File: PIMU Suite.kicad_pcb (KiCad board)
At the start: 2 copper layers, 77 x 50.5 mm, 16 parts, among them U2 MICROSD_SPI_OR_SDIO_CARD

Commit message: Final updates
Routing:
- net /SD_SCK: track 28.5 -> 28.7 mm, vias 2 -> 1
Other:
- board text added: "Made with <3"
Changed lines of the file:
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@@
+		)
+	)
+	(gr_text "Made with <3"
+		(at 181.5 75 0)
+		(layer "B.SilkS")
+		(effects
+			(font
+				(face "Monocraft Nerd Font")
+				(size 1 1)
+				(thickness 0.2)
+				(bold yes)
+			)
+			(justify left bottom mirror)
+		)
+		(render_cache "Made with <3" 0
+			(polygon
+				(pts
+					(xy 181.531263 74.861263) (xy 181.531263 73.708436) (xy 181.313459 73.708436) (xy 181.313459 73.86579)
+					(xy 181.159281 73.86579) (xy 181.159281 74.021067) (xy 181.065919 74.021067) (xy 181.065919 73.86579)
+					(xy 180.908871 73.86579) (xy 180.908871 73.708436) (xy 180.691067 73.708436) (xy 180.691067 74.861263)
+					(xy 180.908871 74.861263) (xy 180.908871 74.083593) (xy 181.003698 74.083593) (xy 181.003698 74.238871)
+					(xy 181.221502 74.238871) (xy 181.221502 74.083593) (xy 181.313459 74.083593) (xy 181.313459 74.861263)
+				)
+			)
+			(polygon
+				(pts
+					(xy 180.441939 74.238871) (xy 179.975863 74.238871) (xy 179.975863 74.333698) (xy 180.441939 74.333698)
+					(xy 180.441939 74.487144) (xy 180.598255 74.487144) (xy 180.598255 74.704947) (xy 180.441939 74.704947)
+					(xy 180.441939 74.861263) (xy 179.75806 74.861263) (xy 179.75806 74.643459) (xy 179.975863 74.643459)
+					(xy 180.380451 74.643459) (xy 180.380451 74.551502) (xy 179.975863 74.551502) (xy 179.975863 74.643459)
+					(xy 179.75806 74.643459) (xy 179.75806 74.176589) (xy 179.914375 74.176589) (xy 179.914375 74.021067)
+					(xy 180.441939 74.021067)
+				)
+			)
+			(polygon
+				(pts
+					(xy 179.042855 74.177383) (xy 179.133775 74.177383) (xy 179.133775 74.021067) (xy 179.508932 74.021067)
+					(xy 179.508932 74.177383) (xy 179.665247 74.177383) (xy 179.665247 74.704947) (xy 179.508932 74.704947)
+					(xy 179.508932 74.861263) (xy 178.825052 74.861263) (xy 178.825052 74.395186) (xy 179.042855 74.395186)
+					(xy 179.042855 74.643459) (xy 179.447444 74.643459) (xy 179.447444 74.238871) (xy 179.196484 74.238871)
+					(xy 179.196484 74.395186) (xy 179.042855 74.395186) (xy 178.825052 74.395186) (xy 178.825052 73.708436)
+					(xy 179.042855 73.708436)
+				)
+			)
+			(polygon
+				(pts
+					(xy 178.575924 74.177383) (xy 178.73224 74.177383) (xy 178.73224 74.704947) (xy 178.575924 74.704947)
+					(xy 178.575924 74.861263) (xy 177.892044 74.861263) (xy 177.892044 74.643459) (xy 178.514436 74.643459)
+					(xy 178.514436 74.551502) (xy 177.892044 74.551502) (xy 177.892044 74.333698) (xy 178.109848 74.333698)
+					(xy 178.514436 74.333698) (xy 178.514436 74.238871) (xy 178.109848 74.238871) (xy 178.109848 74.333698)
+					(xy 177.892044 74.333698) (xy 177.892044 74.177383) (xy 178.04836 74.177383) (xy 178.04836 74.021067)
+					(xy 178.575924 74.021067)
+				)
+			)
+			(polygon
+				(pts
+					(xy 176.710642 74.861263) (xy 176.710642 74.704947) (xy 176.866224 74.704947) (xy 176.866224 74.021067)
+					(xy 176.648421 74.021067) (xy 176.648421 74.643459) (xy 176.556463 74.643459) (xy 176.556463 74.332233)
+					(xy 176.33866 74.332233) (xy 176.33866 74.643459) (xy 176.243832 74.643459) (xy 176.243832 74.021067)
+					(xy 176.026029 74.021067) (xy 176.026029 74.861263)
+				)
+			)
+			(polygon
+				(pts
+					(xy 175.698743 73.92624) (xy 175.698743 73.708436) (xy 175.48094 73.708436) (xy 175.48094 73.92624)
+				)
+			)
+			(polygon
+				(pts
+					(xy 175.542428 74.861263) (xy 175.542428 74.70568) (xy 175.698743 74.70568) (xy 175.698743 74.238871)
+					(xy 175.855059 74.238871) (xy 175.855059 74.021067) (xy 175.48094 74.021067) (xy 175.48094 74.643459)
+					(xy 175.167271 74.643459) (xy 175.167271 74.861263)
+				)
+			)
+			(polygon
+				(pts
+					(xy 174.613328 74.861263) (xy 174.613328 74.704947) (xy 174.765736 74.704947) (xy 174.765736 74.238871)
+					(xy 174.922051 74.238871) (xy 174.922051 74.021067) (xy 174.765736 74.021067) (xy 174.765736 73.708436)
+					(xy 174.547932 73.708436) (xy 174.547932 74.021067) (xy 174.394487 74.021067) (xy 174.394487 74.238871)
+					(xy 174.547932 74.238871) (xy 174.547932 74.643459) (xy 174.238171 74.643459) (xy 174.238171 74.861263)
+				)
+			)
+			(polygon
+				(pts
+					(xy 174.067201 74.861263) (xy 174.067201 73.708436) (xy 173.849398 73.708436) (xy 173.849398 74.177383)
+					(xy 173.758478 74.177383) (xy 173.758478 74.021067) (xy 173.383321 74.021067) (xy 173.383321 74.177383)
+					(xy 173.227006 74.177383) (xy 173.227006 74.861263) (xy 173.444809 74.861263) (xy 173.444809 74.238871)
+					(xy 173.695769 74.238871) (xy 173.695769 74.395186) (xy 173.849398 74.395186) (xy 173.849398 74.861263)
+				)
+			)
+			(polygon
+				(pts
+					(xy 171.735109 74.861263) (xy 171.735109 74.704947) (xy 171.891425 74.704947) (xy 171.891425 74.551502)
+					(xy 172.04487 74.551502) (xy 172.04487 74.395186) (xy 172.201186 74.395186) (xy 172.201186 74.177383)
+					(xy 172.04487 74.177383) (xy 172.04487 74.021067) (xy 171.891425 74.021067) (xy 171.891425 73.86579)
+					(xy 171.735109 73.86579) (xy 171.735109 73.708436) (xy 171.517306 73.708436) (xy 171.517306 73.92624)
+					(xy 171.673621 73.92624) (xy 171.673621 74.083593) (xy 171.827067 74.083593) (xy 171.827067 74.238871)
+					(xy 171.983382 74.238871) (xy 171.983382 74.333698) (xy 171.827067 74.333698) (xy 171.827067 74.487144)
+					(xy 171.673621 74.487144) (xy 171.673621 74.643459) (xy 171.517306 74.643459) (xy 171.517306 74.861263)
+				)
+			)
+			(polygon
+				(pts
+					(xy 171.111863 74.861263) (xy 171.111863 74.704947) (xy 171.268178 74.704947) (xy 171.268178 74.487144)
+					(xy 171.050375 74.487144) (xy 171.050375 74.643459) (xy 170.645786 74.643459) (xy 170.645786 74.395186)
+					(xy 170.959455 74.395186) (xy 170.959455 74.177383) (xy 170.645786 74.177383) (xy 170.645786 73.92624)
+					(xy 171.050375 73.92624) (xy 171.050375 74.082555) (xy 171.268178 74.082555) (xy 171.268178 73.864752)
+					(xy 171.111863 73.864752) (xy 171.111863 73.708436) (xy 170.584298 73.708436) (xy 170.584298 73.864752)
+					(xy 170.427983 73.864752) (xy 170.427983 74.239909) (xy 170.584298 74.239909) (xy 170.584298 74.32979)
+					(xy 170.427983 74.32979) (xy 170.427983 74.704947) (xy 170.584298 74.704947) (xy 170.584298 74.861263)
+				)
+			)
+		)
+	)
+	(gr_text_box "Next version:\n- Add silkscreen names to each pin\n- Cleanup routes\n- Change meme"
+		(start 130.125 61.375)
+		(end 164.375 69.625)
+		(margins 1.0025 1.0025 1.0025 1.0025)
+		(layer "F.Fab")
+		(effects
+			(font
+				(size 1 1)
+				(thickness 0.2)
+				(bold yes)
+			)
+			(justify left top)
+		)
+		(border yes)
+		(stroke
+			(width 0.2)
+			(type solid)
 		)
 	)
@@
 	)
 	(segment
-		(start 131.5 95.5)
-		(end 131.75 95.25)
-		(width 0.2)
-		(layer "F.Cu")
-		(net 19)
-	)
-	(segment
 		(start 131.75 89.93)
 		(end 143.22 78.46)
@@
 	)
 	(segment
-		(start 127.08 99.92)
-		(end 127.875 99.125)
-		(width 0.2)
-		(layer "F.Cu")
-		(net 19)
-	)
-	(segment
 		(start 131.75 95.25)
 		(end 131.75 89.93)
@@
 	)
 	(via
-		(at 127.875 99.125)
+		(at 131.75 95.25)
 		(size 0.7)
 		(drill 0.3)
@@
 		(net 19)
 	)
-	(via
-		(at 131.5 95.5)
-		(size 0.6)
-		(drill 0.3)
-		(layers "F.Cu" "B.Cu")
-		(net 19)
-	)
-	(segment
-		(start 127.875 99.125)
-		(end 131.5 95.5)
+	(segment
+		(start 131.75 95.25)
+		(end 131.75 95.44)
 		(width 0.2)
 		(layer "B.Cu")
@@
 		(width 0.2)
 		(layer "B.Cu")
+		(net 19)
+	)
+	(segment
+		(start 131.75 95.44)
+		(end 127.08 100.11)
+		(width 0.2)
+		(layer "B.Cu")

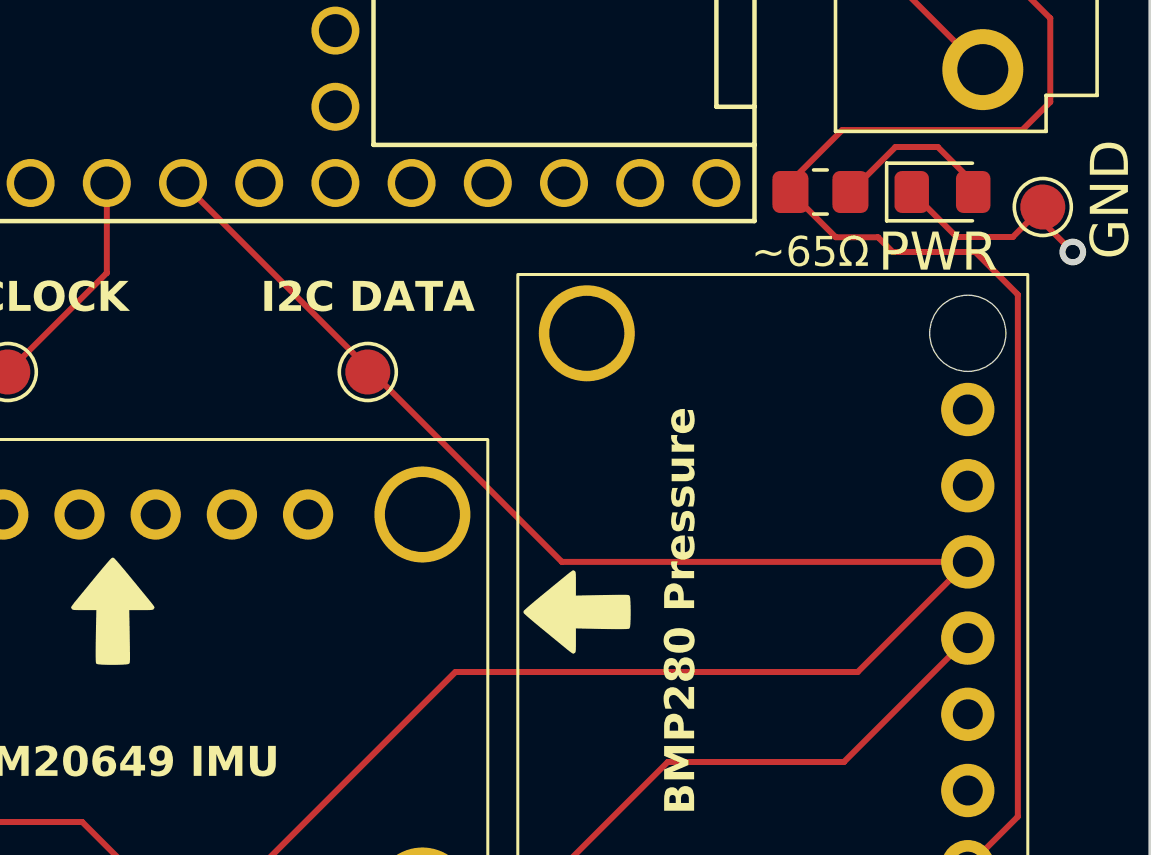
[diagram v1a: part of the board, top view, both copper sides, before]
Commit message: Fix wrong wiring
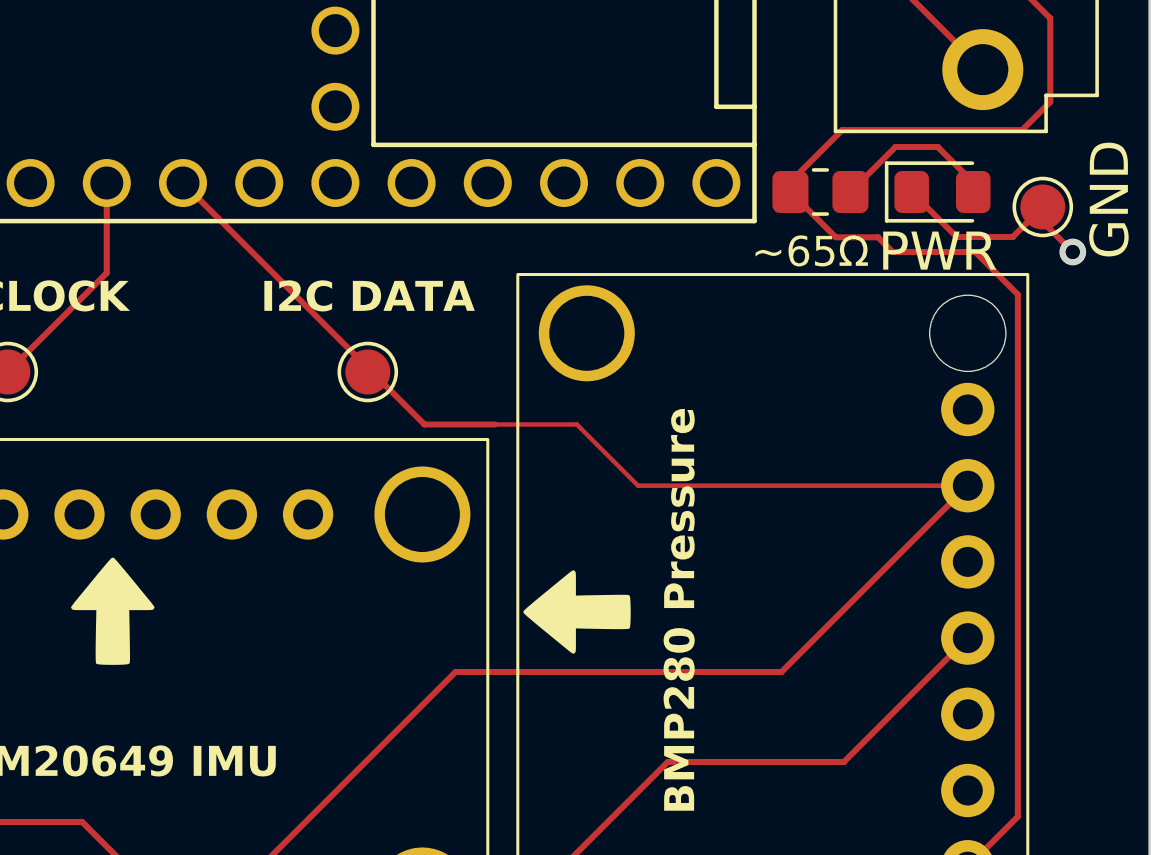
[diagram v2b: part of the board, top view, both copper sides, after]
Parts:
- JST1: value JST -> S4B-XH-A-1
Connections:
- BMP1 pad 5: /SDA_LINE -> unconnected-(BMP1-SDO-Pad5)
- BMP1 pad 6: unconnected-(BMP1-SDI-Pad6) -> /SDA_LINE
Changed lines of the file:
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@@
 	(net 68 "unconnected-(TEENSY1-GND-Pad58)")
 	(net 69 "unconnected-(U2-DAT2-Pad8)")
-	(net 70 "unconnected-(BMP1-SDI-Pad6)")
+	(net 70 "unconnected-(BMP1-SDO-Pad5)")
 	(net 71 "unconnected-(U2-DAT1-Pad7)")
 	(net 72 "unconnected-(TEENSY1-T--Pad62)")
@@
 			)
 		)
-		(property "Value" "JST"
+		(property "Value" "S4B-XH-A-1"
 			(at 5.94 6 90)
 			(layer "F.Fab")
@@
 			(layers "*.Cu" "*.Mask")
 			(remove_unused_layers no)
-			(net 11 "/SDA_LINE")
+			(net 70 "unconnected-(BMP1-SDO-Pad5)")
 			(pinfunction "SDO")
 			(pintype "output")
@@
 			(layers "*.Cu" "*.Mask")
 			(remove_unused_layers no)
-			(net 70 "unconnected-(BMP1-SDI-Pad6)")
+			(net 11 "/SDA_LINE")
 			(pinfunction "SDI")
 			(pintype "input")
@@
 	)
 	(segment
-		(start 177 106.33)
-		(end 173.33 110)
+		(start 150.84 93.7)
+		(end 158.89 101.75)
 		(width 0.2)
 		(layer "F.Cu")
@@
 	)
 	(segment
-		(start 150.84 93.7)
-		(end 163.47 106.33)
+		(start 159.92 110)
+		(end 152.47 117.45)
 		(width 0.2)
 		(layer "F.Cu")
@@
 	)
 	(segment
-		(start 159.92 110)
-		(end 152.47 117.45)
-		(width 0.2)
+		(start 161.25 101.75)
+		(end 163.97 101.75)
+		(width 0.15)
 		(layer "F.Cu")
 		(net 11)
 	)
 	(segment
-		(start 177 106.33)
-		(end 177 106)
+		(start 158.89 101.75)
+		(end 161.25 101.75)
 		(width 0.2)
 		(layer "F.Cu")
@@
 	)
 	(segment
-		(start 173.33 110)
+		(start 166.01 103.79)
+		(end 177 103.79)
+		(width 0.15)
+		(layer "F.Cu")
+		(net 11)
+	)
+	(segment
+		(start 170.79 110)
 		(end 159.92 110)
 		(width 0.2)
@@
 	)
 	(segment
-		(start 163.47 106.33)
-		(end 177 106.33)
+		(start 177 103.79)
+		(end 170.79 110)
 		(width 0.2)
 		(layer "F.Cu")
@@
 	)
 	(segment
+		(start 163.97 101.75)
+		(end 166.01 103.79)
+		(width 0.15)
+		(layer "F.Cu")
+		(net 11)
+	)
+	(segment
 		(start 127.08 100.11)
 		(end 127.08 99.92)
@@
 	)
 	(segment
+		(start 177 106.33)
+		(end 177 106)
+		(width 0.2)
+		(layer "F.Cu")
+		(net 70)
+	)
+	(segment

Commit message: JLCPCB specs
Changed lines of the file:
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@@
 		)
 		(pad_to_mask_clearance 0)
+		(solder_mask_min_width 0.12)
 		(allow_soldermask_bridges_in_footprints no)
 		(tenting front back)
 		(pcbplotparams
 			(layerselection 0x00000000_00000000_55555555_5755f5ff)
-			(plot_on_all_layers_selection 0x00000000_00000000_00000000_0200a0af)
+			(plot_on_all_layers_selection 0x00000000_00000000_00000000_00000000)
 			(disableapertmacros no)
 			(usegerberextensions no)
@@
 			(dashed_line_gap_ratio 3.000000)
 			(svgprecision 4)
-			(plotframeref yes)
+			(plotframeref no)
 			(mode 1)
 			(useauxorigin no)
@@
 			(pdf_back_fp_property_popups yes)
 			(pdf_metadata yes)
-			(pdf_single_document yes)
+			(pdf_single_document no)
 			(dxfpolygonmode yes)
 			(dxfimperialunits yes)
@@
 			(psnegative no)
 			(psa4output no)
-			(plot_black_and_white no)
+			(plot_black_and_white yes)
 			(sketchpadsonfab no)
 			(plotpadnumbers no)
@@
 			(crossoutdnponfab yes)
 			(subtractmaskfromsilk no)
-			(outputformat 4)
+			(outputformat 1)
 			(mirror no)
 			(drillshape 0)
 			(scaleselection 1)
-			(outputdirectory "Board Versions/")
+			(outputdirectory "Drills/")
 		)
 	)
@@
 				(font
 					(size 1 1)
-					(thickness 0.125)
+					(thickness 0.15)
 				)
 			)
@@
 		(effects
 			(font
-				(size 0.8 0.8)
+				(size 1 1)
 				(thickness 0.1875)
 				(bold yes)
@@
 		(effects
 			(font
-				(size 0.8 0.8)
+				(size 1 1)
 				(thickness 0.1875)
 				(bold yes)
@@
 	)
 	(segment
+		(start 131.75 95.44)
+		(end 131.75 89.93)
+		(width 0.2)
+		(layer "F.Cu")
+		(net 19)
+	)
+	(segment
 		(start 127.08 100.11)
 		(end 127.08 99.92)
@@
 	)
 	(segment
-		(start 131.75 89.93)
-		(end 143.22 78.46)
+		(start 131.47 95.72)
+		(end 131.75 95.44)
 		(width 0.2)
 		(layer "F.Cu")
@@
 	)
 	(segment
-		(start 131.75 95.25)
-		(end 131.75 89.93)
+		(start 131.75 89.93)
+		(end 143.22 78.46)
 		(width 0.2)
 		(layer "F.Cu")
@@
 	)
 	(via
-		(at 131.75 95.25)
+		(at 131.47 95.72)
 		(size 0.7)
 		(drill 0.3)
@@
 	)
 	(segment
-		(start 131.75 95.25)
-		(end 131.75 95.44)
+		(start 131.47 95.72)
+		(end 127.08 100.11)
 		(width 0.2)
 		(layer "B.Cu")
@@
 		(width 0.2)
 		(layer "B.Cu")
-		(net 19)
-	)
-	(segment
-		(start 131.75 95.44)
-		(end 127.08 100.11)
-		(width 0.2)
-		(layer "B.Cu")

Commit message: Fillits and bore holes:
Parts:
- added REF**: MountingHole_2.7mm_M2.5, MountingHole:MountingHole_2.7mm_M2.5, F.Cu at (188.5, 131.5)
- added REF**: MountingHole_2.7mm_M2.5, MountingHole:MountingHole_2.7mm_M2.5, F.Cu at (104.5, 71.5)
- added REF**: MountingHole_2.7mm_M2.5, MountingHole:MountingHole_2.7mm_M2.5, F.Cu at (188.5, 71.5)
- added REF**: MountingHole_2.7mm_M2.5, MountingHole:MountingHole_2.7mm_M2.5, F.Cu at (104.5, 131.5)
- moved G*** 4.82 mm to (111.1, 79.2)
- moved G*** 4.82 mm to (123.6, 122.2)
- moved G*** 4.82 mm to (119.6, 112.2)
- moved TP1 4.82 mm to (120.6, 79.7)
- moved U2 4.82 mm to (123.1, 113.7)
- moved BMP1 4.82 mm to (170.6, 112.9)
- moved D1 4.82 mm to (177.2, 98.7)
- moved G*** 4.82 mm to (165.1, 112.7)
- moved G*** 4.82 mm to (149.6, 112.7)
- moved IMU1 4.82 mm to (149.6, 114.9)
- moved JST1 4.82 mm to (178.6, 82.7)
- moved R1 4.82 mm to (173.2, 98.7)
- moved TEENSY1 4.82 mm to (140.5, 90.8)
- moved TP2 4.82 mm to (180.6, 99.2)
- moved TP3 4.82 mm to (146.1, 104.7)
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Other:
- board size 77 x 50.5 mm -> 93 x 69 mm

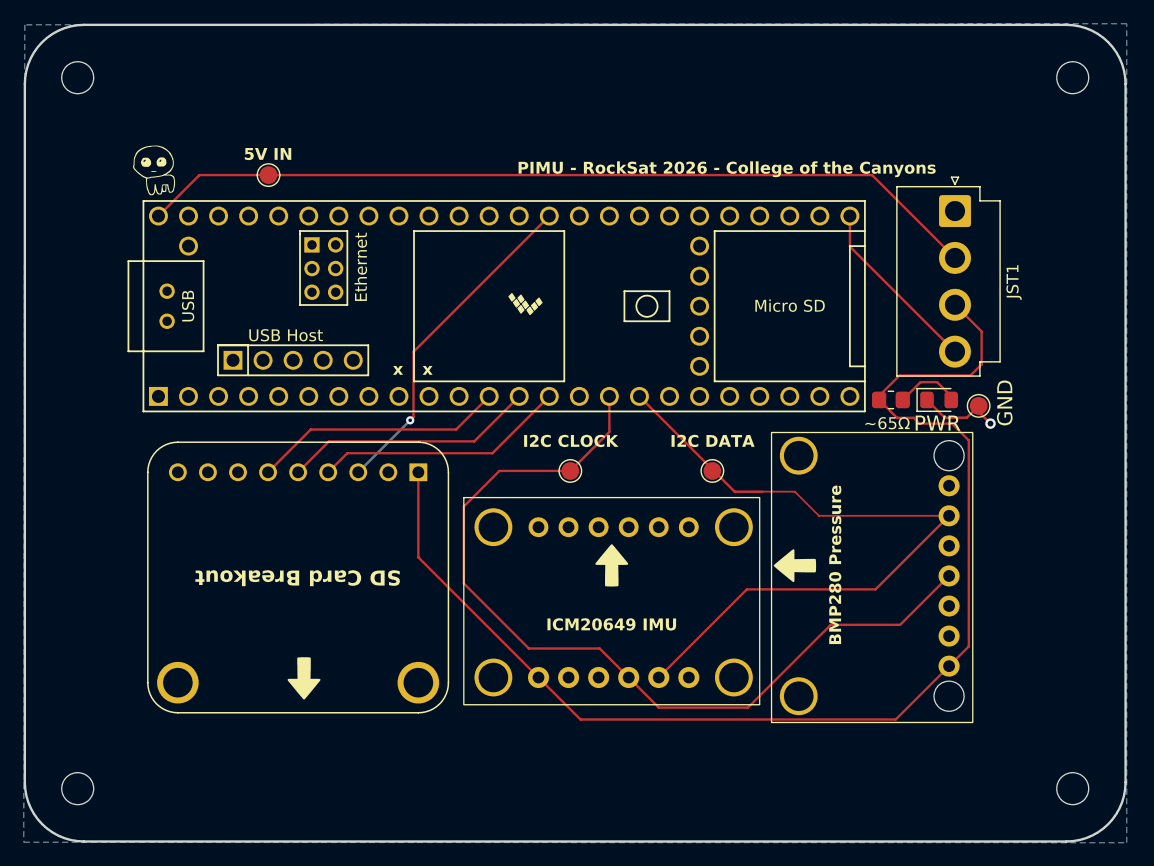
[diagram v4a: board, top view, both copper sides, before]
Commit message: Move JST
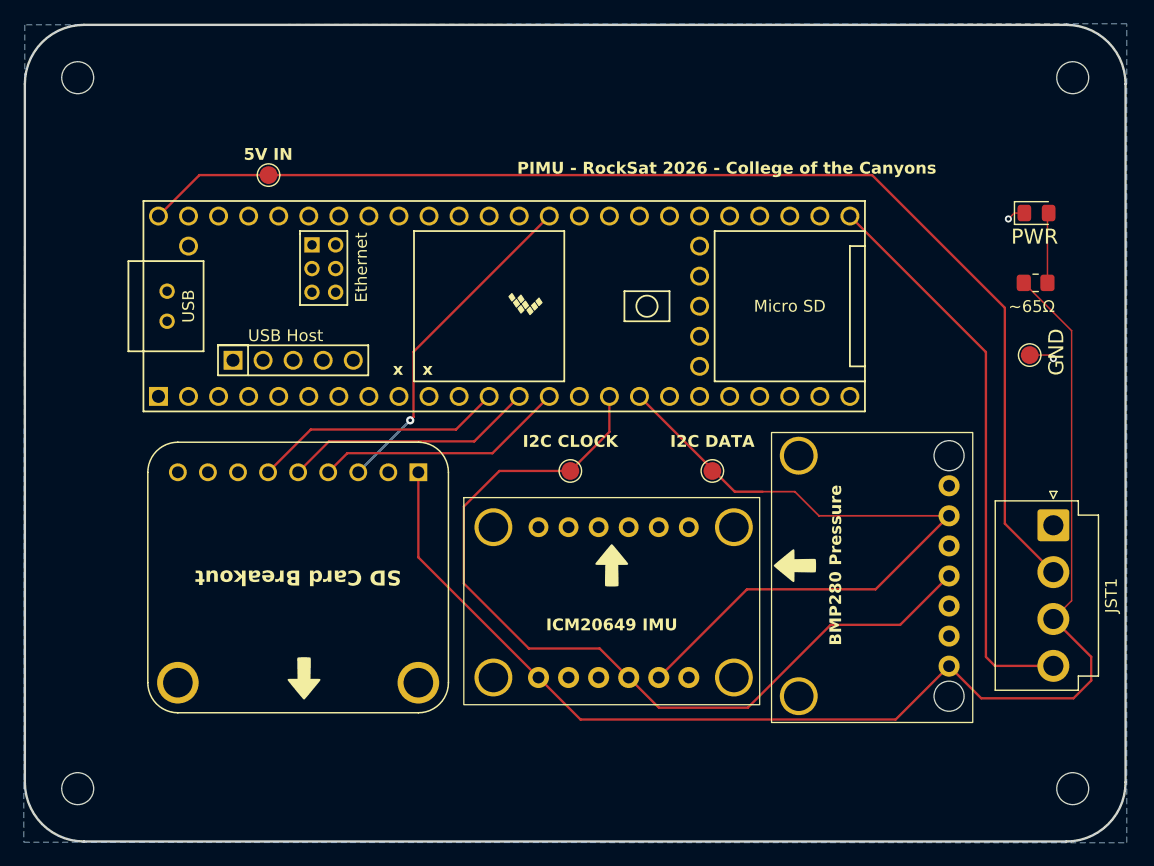
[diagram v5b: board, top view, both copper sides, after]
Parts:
- removed the G*** at (111.1, 79.2)
- moved JST1 27.8 mm to (186.9, 109.3)
- moved D1 17.8 mm to (185.5, 82.9)
- moved R1 15.7 mm to (185.4, 88.8)
- moved TP2 6.08 mm to (184.9, 94.9)
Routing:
- net /TE: track 15.1 -> 48.0 mm
- net +5V: track 71.6 -> 101.6 mm
- net +3.3V: track 104.5 -> 110.6 mm
- net GND: track 7.32 -> 3.68 mm, vias 1 -> 2

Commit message: tx rx
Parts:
- added TP5: 3V3, TestPoint:TestPoint_Pad_D1.5mm, F.Cu at (189.9, 98.4)
- added TP6: TE, TestPoint:TestPoint_Pad_D1.5mm, F.Cu at (179.1, 95.9)
- added TP7: TX, TestPoint:TestPoint_Pad_D1.5mm, F.Cu at (175.5, 98.7)
- added TP8: RX, TestPoint:TestPoint_Pad_D1.5mm, F.Cu at (173.5, 83.6)
- JST1: value S4B-XH-A-1 -> JST_VH_B6P-VH-B; footprint Connector_JST:JST_VH_B4P-VH-B_1x04_P3.96mm_Vertical -> Connector_JST:JST_VH_B6P-VH-B_1x06_P3.96mm_Vertical
- moved JST1 5.61 mm to (187.5, 103.7)
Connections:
- TEENSY1 pad 26: unconnected-(TEENSY1-34_RX8-Pad26) -> /UART_TO_TEENSY
- TEENSY1 pad 27: unconnected-(TEENSY1-35_TX8-Pad27) -> /UART_FROM_TEENSY
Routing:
- net /UART_FROM_TEENSY: track 0.00 -> 53.4 mm, vias 0 -> 2
- net /UART_TO_TEENSY: track 0.00 -> 53.4 mm, vias 0 -> 2
- net +3.3V: track 110.6 -> 99.1 mm
- net /TE: track 48.0 -> 41.2 mm, vias 0 -> 2
- net +5V: track 101.6 -> 96.3 mm
